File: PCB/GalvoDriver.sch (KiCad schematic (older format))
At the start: 25 parts, among them J1 Screw_Terminal_01x03, J2 Conn_01x03, J3 Conn_01x06_Male, J4 JUMPER_A, J5 JUMPER_B, J6 AudioJack3, J7 Conn_01x03, U1 TL082, U2 MCP4822, U3 TL082

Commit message: Added Laser Module Control + terminal
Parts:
- added J8: Screw_Terminal_01x04, TerminalBlocks_Phoenix:TerminalBlock_Phoenix_MKDS1.5-4pol, symbol Connector:Screw_Terminal_01x04
- added Q1: PN2222A, TO_SOT_Packages_THT:TO-92_Inline_Narrow_Oval, symbol Transistor_BJT:PN2222A
- added R11: 100, Resistors_THT:R_Axial_DIN0207_L6.3mm_D2.5mm_P10.16mm_Horizontal, symbol Device:R_US
- J1: footprint TerminalBlocks_Phoenix:TerminalBlock_Phoenix_PT-3.5mm_3pol -> TerminalBlocks_Phoenix:TerminalBlock_Phoenix_MKDS1.5-3pol
- J3: value Conn_01x06_Male -> Conn_01x07_Male; footprint Pin_Headers:Pin_Header_Straight_1x06_Pitch2.54mm -> Pin_Headers:Pin_Header_Straight_1x07_Pitch2.54mm; symbol Connector:Conn_01x06_Male -> Connector:Conn_01x07_Male
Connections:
- net GND: now also J8.3 (Pin_3), Q1.1 (E)
- new net: J8.1 (Pin_1), Q1.3 (C)
- new net: Q1.2 (B), R11.1
- new net LASER: J3.7 (Pin_7), R11.2
- new net VSS: J8.2 (Pin_2), J8.4 (Pin_4)
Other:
- note added: "Connector Labels:\n1 - 3V3-5V\n2 - CLK\n3 - LATCH\n4 - MOSI\n5 - CS\n6 - LASER\n7 - GND"
- note added: "Connector Labels:\n4 - V+\n3 - GND\n2 - Laser +\n1 - Laser -"
- note added: "Laser Module\nControl"
- note removed: "Connector Labels:\n1 - 3V3-5V\n2 - CLK\n3 - LATCH\n4 - MOSI\n5 - CS\n6 - GND"
- moved on the sheet: J2, J4, J5, J7, R1, R10, R2, R3, R4, R5, R6, R7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

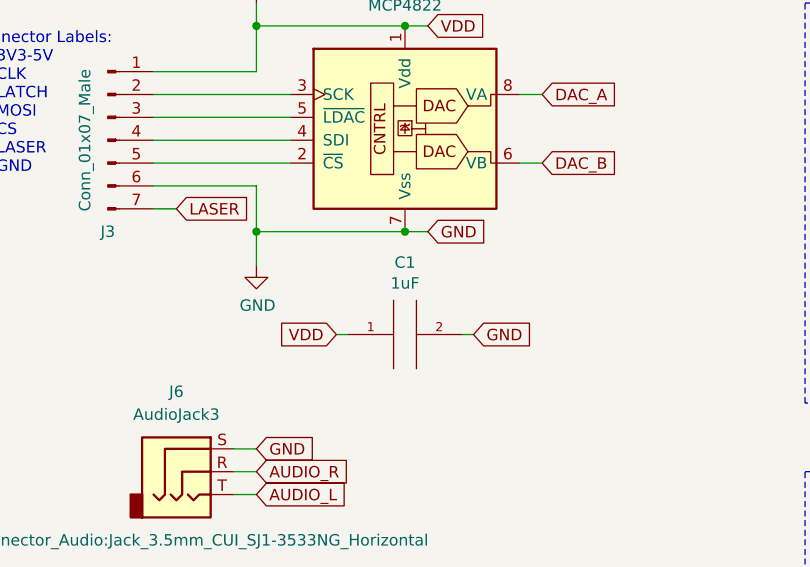
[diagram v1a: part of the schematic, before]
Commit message: Changed decoupling cap value to 0.1uF
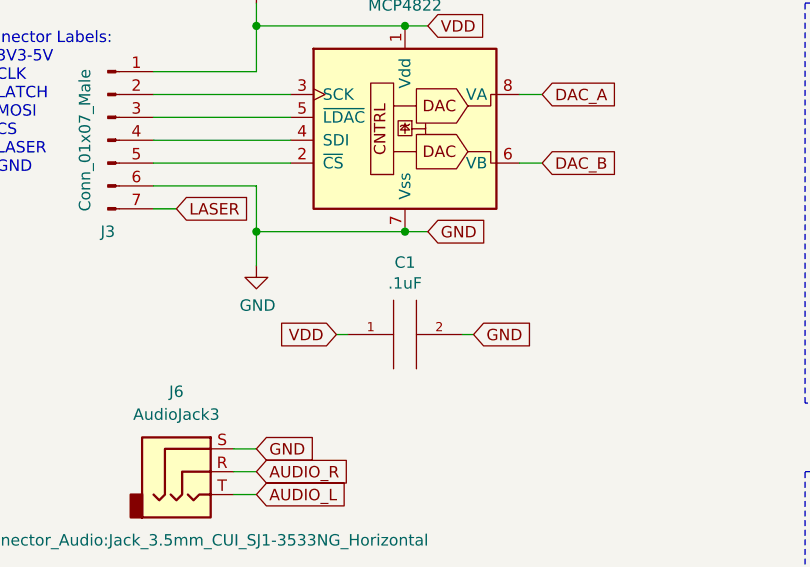
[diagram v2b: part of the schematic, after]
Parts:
- C1: value 1uF -> .1uF; DigiKey (none) -> https://www.digikey.com/product-detail/en/vishay-bc-compone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
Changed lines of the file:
@@
 P 2550 3350
 F 0 "C1" V 2865 3350 50  0000 C CNN
-F 1 "1uF" V 2774 3350 50  0000 C CNN
+F 1 ".1uF" V 2774 3350 50  0000 C CNN
 F 2 "Capacitors_THT:C_Disc_D5.0mm_W2.5mm_P2.50mm" H 2550 3350 50  0001 C CNN
 F 3 "~" H 2550 3350 50  0001 C CNN
+F 4 "https://www.digikey.com/product-detail/en/vishay-bc-components/K104Z15Y5VF5TL2/BC1160CT-ND/286782" V 2550 3350 50  0001 C CNN "DigiKey"
 	1    2550 3350
 	0    -1   -1   0

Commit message: Starting work on PCB changes for v1.1
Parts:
- removed J3: Conn_01x07_Male, Pin_Headers:Pin_Header_Straight_1x07_Pitch2.54mm, symbol Connector:Conn_01x07_Male
- added J?: Conn_01x05_Male, symbol Connector:Conn_01x05_Male
- added U?: 74AHC125, symbol 74ahc125:74AHC125
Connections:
- wire segments 107 -> 110
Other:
- note added: "Connector Labels:\n1 - 3V3-5V\n2 - CLK\n3 - MOSI\n4 - LASER\n5 - GND"
- note removed: "Connector Labels:\n1 - 3V3-5V\n2 - CLK\n3 - LATCH\n4 - MOSI\n5 - CS\n6 - LASER\n7 - GND"
- moved on the sheet: J6
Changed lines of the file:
@@
 Wire Wire Line
 	1700 1450 1600 1450
-$Comp
-L Connector:Conn_01x07_Male J3
-U 1 1 5EFED4AC
-P 1250 2500
-F 0 "J3" H 1250 2100 50  0000 C CNN
-F 1 "Conn_01x07_Male" V 1150 2500 50  0000 C CNN
-F 2 "Pin_Headers:Pin_Header_Straight_1x07_Pitch2.54mm" H 1250 2500 50  0001 C CNN
-F 3 "~" H 1250 2500 50  0001 C CNN
-	1    1250 2500
-	1    0    0    -1
-$EndComp
 Wire Wire Line
 	1900 2200 1900 2000
@@
 	1900 2700 1900 2900
 Wire Wire Line
-	1900 2900 2550 2900
-Text Notes 650  2650 0    50   ~ 0
-Connector Labels:\n1 - 3V3-5V\n2 - CLK\n3 - LATCH\n4 - MOSI\n5 - CS\n6 - LASER\n7 - GND
+	1900 2900 2000 2900
+Text Notes 700  4250 0    50   ~ 0
+Connector Labels:\n1 - 3V3-5V\n2 - CLK\n3 - MOSI\n4 - LASER\n5 - GND
 Text GLabel 8650 2800 0    50   Input ~ 0
 A_ILDA+
@@
 Wire Wire Line
 	2850 3350 2800 3350
-Text GLabel 1900 3950 2    50   Input ~ 0
+Text GLabel 2600 6550 2    50   Input ~ 0
 AUDIO_R
-Text GLabel 1900 3850 2    50   Input ~ 0
-GND
-Text GLabel 1900 4050 2    50   Input ~ 0
+Text GLabel 2600 6450 2    50   Input ~ 0
+GND
+Text GLabel 2600 6650 2    50   Input ~ 0
 AUDIO_L
 Text GLabel 4750 2800 0    50   Input ~ 0
@@
 L Connector:AudioJack3 J6
 U 1 1 5EF780C5
-P 1600 3950
-F 0 "J6" H 1550 4300 50  0000 C CNN
-F 1 "AudioJack3" H 1550 4200 50  0000 C CNN
-F 2 "Connector_Audio:Jack_3.5mm_CUI_SJ1-3533NG_Horizontal" H 1650 3650 50  0000 C CNN
-F 3 "https://www.cuidevices.com/product/resource/sj1-353xng.pdf" H 1600 3950 50  0001 C CNN
-F 4 "https://www.digikey.com/product-detail/en/cui-devices/SJ1-3533NG/CP1-3533NG-ND/738701" H 1600 3950 50  0001 C CNN "DigiKey"
-	1    1600 3950
-	1    0    0    -1
-$EndComp
-Wire Wire Line
-	1900 3850 1800 3850
-Wire Wire Line
-	1800 3950 1900 3950
-Wire Wire Line
-	1900 4050 1800 4050
+P 2300 6550
+F 0 "J6" H 2250 6900 50  0000 C CNN
+F 1 "AudioJack3" H 2250 6800 50  0000 C CNN
+F 2 "Connector_Audio:Jack_3.5mm_CUI_SJ1-3533NG_Horizontal" H 2350 6250 50  0000 C CNN
+F 3 "https://www.cuidevices.com/product/resource/sj1-353xng.pdf" H 2300 6550 50  0001 C CNN
+F 4 "https://www.digikey.com/product-detail/en/cui-devices/SJ1-3533NG/CP1-3533NG-ND/738701" H 2300 6550 50  0001 C CNN "DigiKey"
+	1    2300 6550
+	1    0    0    -1
+$EndComp
+Wire Wire Line
+	2600 6450 2500 6450
+Wire Wire Line
+	2500 6550 2600 6550
+Wire Wire Line
+	2600 6650 2500 6650
 $Comp
 L Connector:Conn_01x03_Male J5
@@
 	1450 2300 2050 2300
 Wire Wire Line
-	1450 2400 2050 2400
-Wire Wire Line
 	1450 2500 2050 2500
-Wire Wire Line
-	1450 2600 2050 2600
 Wire Wire Line
 	1450 2700 1900 2700
@@
 	5750 950  5900 950
 Connection ~ 5900 950
+$Comp
+L 74ahc125:74AHC125 U?
+U 1 1 5F28DEB8
+P 2550 4650
+F 0 "U?" H 2550 5465 50  0000 C CNN
+F 1 "74AHC125" H 2550 5374 50  0000 C CNN
+F 2 "" H 2550 4650 60  0000 C CNN
+F 3 "" H 2550 4650 60  0000 C CNN
+	1    2550 4650
+	1    0    0    -1
+$EndComp
+Wire Wire Line
+	2050 2400 2000 2400
+Wire Wire Line
+	2000 2400 2000 2900
+Connection ~ 2000 2900
+Wire Wire Line
+	2000 2900 2050 2900
+Wire Wire Line
+	2050 2600 2050 2900
+Connection ~ 2050 2900
+Wire Wire Line
+	2050 2900 2550 2900
+$Comp
+L Connector:Conn_01x05_Male J?
+U 1 1 5F2A1C2E
+P 1250 4750
+F 0 "J?" H 1358 5131 50  0000 C CNN
+F 1 "Conn_01x05_Male" H 1358 5040 50  0000 C CNN
+F 2 "" H 1250 4750 50  0001 C CNN
+F 3 "~" H 1250 4750 50  0001 C CNN
+	1    1250 4750
+	1    0    0    -1
+$EndComp
 $EndSCHEMATC

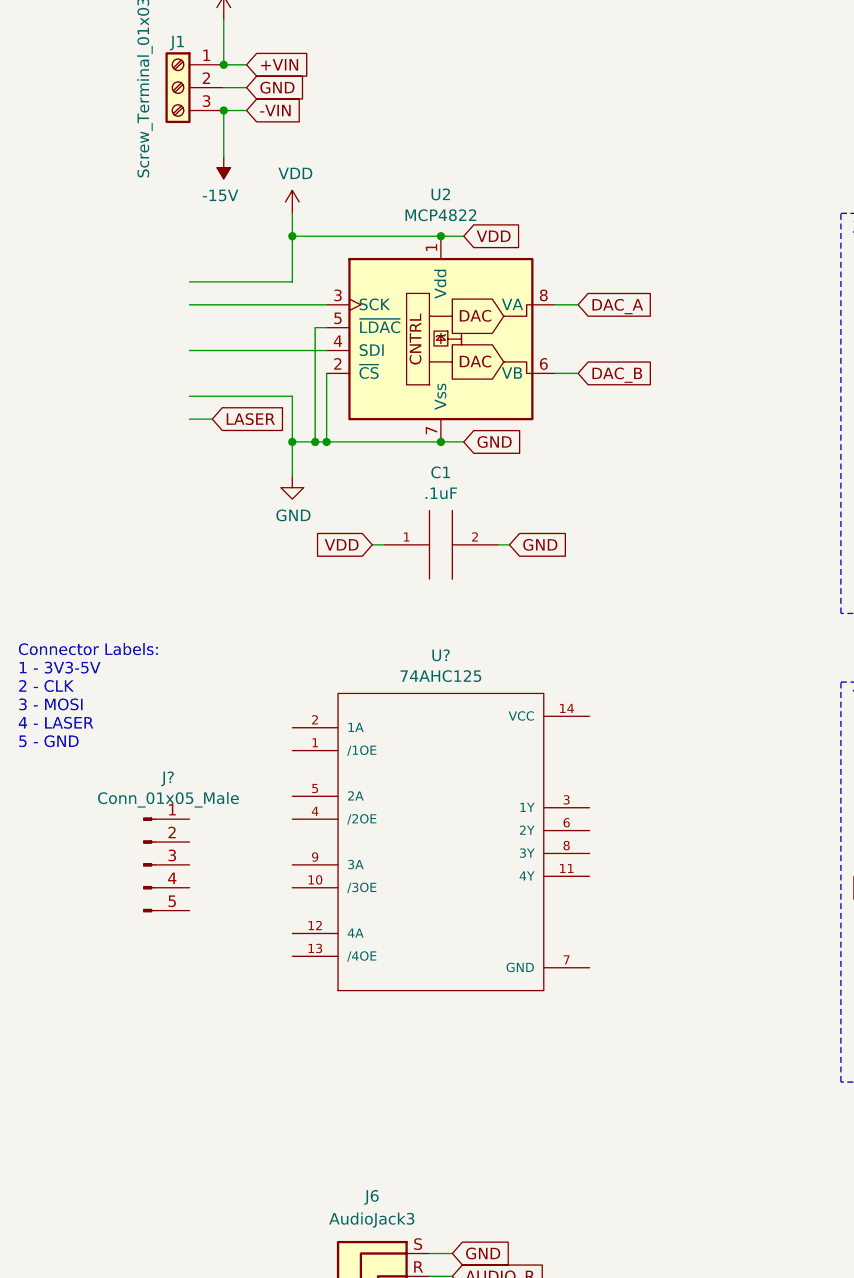
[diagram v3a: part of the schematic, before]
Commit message: Level shifter, thrm. relief, xistor pad, audio jack move
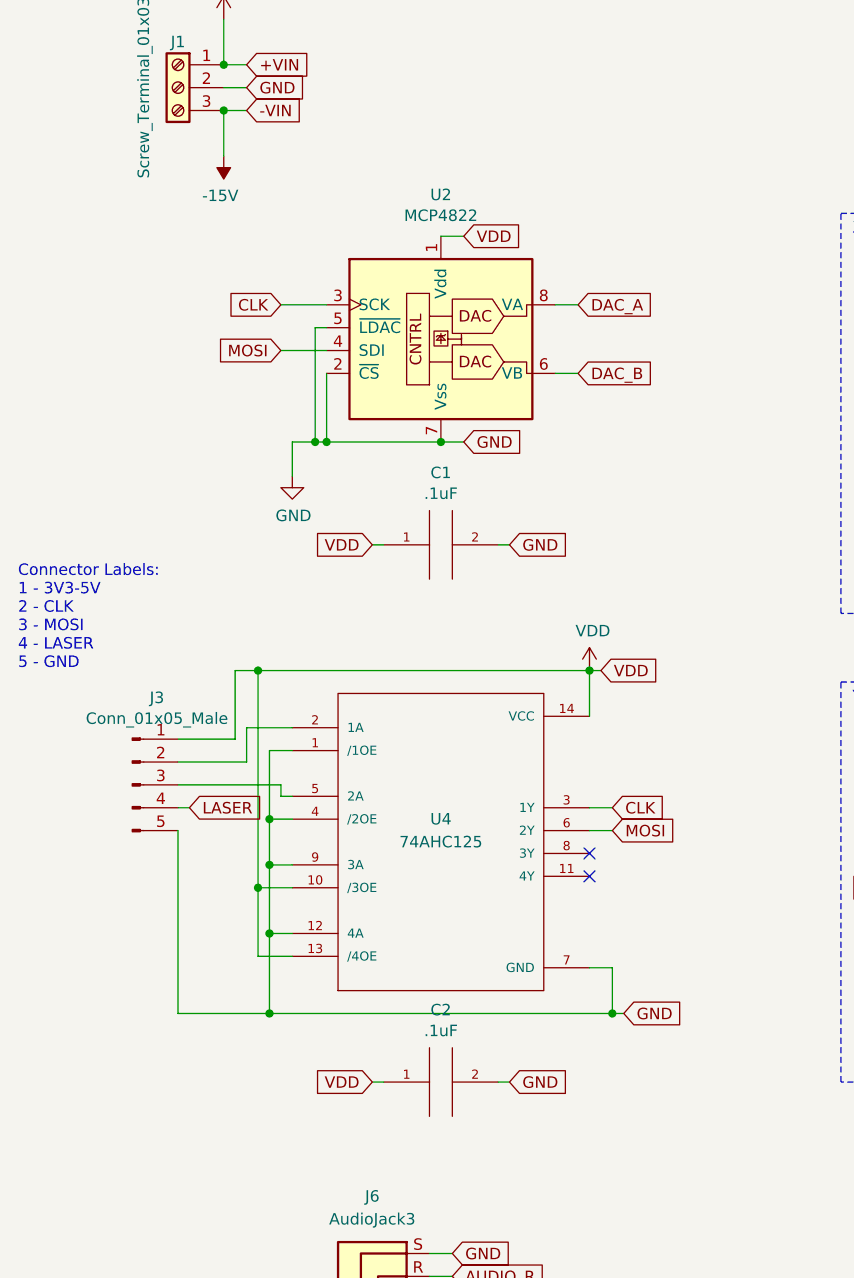
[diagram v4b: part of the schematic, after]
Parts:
- added C2: .1uF, Capacitors_THT:C_Disc_D5.0mm_W2.5mm_P2.50mm, symbol pspice:C
- J3: renamed from J?; footprint (none) -> Pin_Headers:Pin_Header_Straight_1x05_Pitch2.54mm
- Q1: footprint TO_SOT_Packages_THT:TO-92_Inline_Narrow_Oval -> TO_SOT_Packages_THT:TO-92_Inline_Wide
- U4: renamed from U?; footprint (none) -> Housings_DIP:DIP-14_W7.62mm_Socket; DigiKey (none) -> https://www.digikey.com/product-detail/en/texas-instruments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
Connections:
- net labels added: CLK, MOSI
- wire segments 110 -> 138
- no-connect marks 2 -> 4
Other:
- moved on the sheet: J3
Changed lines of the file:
@@
 	1700 1450 1600 1450
 Wire Wire Line
-	1900 2200 1900 2000
-Wire Wire Line
-	1900 2000 2550 2000
-Wire Wire Line
-	1900 2700 1900 2900
-Wire Wire Line
 	1900 2900 2000 2900
-Text Notes 700  4250 0    50   ~ 0
+Text Notes 700  3900 0    50   ~ 0
 Connector Labels:\n1 - 3V3-5V\n2 - CLK\n3 - MOSI\n4 - LASER\n5 - GND
 Text GLabel 8650 2800 0    50   Input ~ 0
@@
 L power:VDD #PWR0101
 U 1 1 5F007EE1
-P 1900 1900
-F 0 "#PWR0101" H 1900 1750 50  0001 C CNN
-F 1 "VDD" H 1915 2073 50  0000 C CNN
-F 2 "" H 1900 1900 50  0001 C CNN
-F 3 "" H 1900 1900 50  0001 C CNN
-	1    1900 1900
+P 3200 3900
+F 0 "#PWR0101" H 3200 3750 50  0001 C CNN
+F 1 "VDD" H 3215 4073 50  0000 C CNN
+F 2 "" H 3200 3900 50  0001 C CNN
+F 3 "" H 3200 3900 50  0001 C CNN
+	1    3200 3900
 	1    0    0    -1
 $EndComp
@@
 Wire Wire Line
 	1900 3050 1900 2900
-Connection ~ 1900 2900
-Wire Wire Line
-	1900 1900 1900 2000
-Connection ~ 1900 2000
 Wire Wire Line
 	5800 3200 6400 3200
@@
 Wire Wire Line
 	2650 2000 2550 2000
-Connection ~ 2550 2000
 Text GLabel 2250 3350 0    50   Input ~ 0
 VDD
@@
 Wire Wire Line
 	8650 5050 8750 5050
-Text GLabel 1550 2800 2    50   Input ~ 0
-LASER
-Wire Wire Line
-	1450 2200 1900 2200
-Wire Wire Line
-	1450 2300 2050 2300
-Wire Wire Line
-	1450 2500 2050 2500
-Wire Wire Line
-	1450 2700 1900 2700
-Wire Wire Line
-	1550 2800 1450 2800
 $Comp
 L Connector:Screw_Terminal_01x04 J8
@@
 F 0 "Q1" H 6290 1446 50  0000 L CNN
 F 1 "PN2222A" H 6290 1355 50  0000 L CNN
-F 2 "TO_SOT_Packages_THT:TO-92_Inline_Narrow_Oval" H 6300 1325 50  0001 L CIN
+F 2 "TO_SOT_Packages_THT:TO-92_Inline_Wide" H 6300 1325 50  0001 L CIN
 F 3 "http://www.fairchildsemi.com/ds/PN/PN2222A.pdf" H 6100 1400 50  0001 L CNN
 	1    6100 1400
@@
 Connection ~ 5900 950
 $Comp
-L 74ahc125:74AHC125 U?
+L 74ahc125:74AHC125 U4
 U 1 1 5F28DEB8
 P 2550 4650
-F 0 "U?" H 2550 5465 50  0000 C CNN
-F 1 "74AHC125" H 2550 5374 50  0000 C CNN
-F 2 "" H 2550 4650 60  0000 C CNN
-F 3 "" H 2550 4650 60  0000 C CNN
+F 0 "U4" H 2550 4750 50  0000 C CNN
+F 1 "74AHC125" H 2550 4650 50  0000 C CNN
+F 2 "Housings_DIP:DIP-14_W7.62mm_Socket" H 2550 4650 60  0001 C CNN
+F 3 "http://www.ti.com/general/docs/suppproductinfo.tsp?distId=10&gotoUrl=http%3A%2F%2Fwww.ti.com%2Flit%2Fgpn%2Fsn74ahc125" H 2550 4650 60  0001 C CNN
+F 4 "https://www.digikey.com/product-detail/en/texas-instruments/SN74AHC125N/296-4531-5-ND/375724" H 2550 4650 50  0001 C CNN "DigiKey"
 	1    2550 4650
 	1    0    0    -1
@@
 	2050 2900 2550 2900
 $Comp
-L Connector:Conn_01x05_Male J?
+L Connector:Conn_01x05_Male J3
 U 1 1 5F2A1C2E
-P 1250 4750
-F 0 "J?" H 1358 5131 50  0000 C CNN
-F 1 "Conn_01x05_Male" H 1358 5040 50  0000 C CNN
-F 2 "" H 1250 4750 50  0001 C CNN
-F 3 "~" H 1250 4750 50  0001 C CNN
-	1    1250 4750
-	1    0    0    -1
-$EndComp
+P 1200 4400
+F 0 "J3" H 1308 4781 50  0000 C CNN
+F 1 "Conn_01x05_Male" H 1308 4690 50  0000 C CNN
+F 2 "Pin_Headers:Pin_Header_Straight_1x05_Pitch2.54mm" H 1200 4400 50  0001 C CNN
+F 3 "~" H 1200 4400 50  0001 C CNN
+	1    1200 4400
+	1    0    0    -1
+$EndComp
+Wire Wire Line
+	1900 4250 1800 4250
+Wire Wire Line
+	1800 5400 3300 5400
+Wire Wire Line
+	3300 5400 3300 5200
+Wire Wire Line
+	3300 5200 3200 5200
+Text GLabel 3350 5400 2    50   Input ~ 0
+GND
+Wire Wire Line
+	3300 5400 3350 5400
+Connection ~ 3300 5400
+Wire Wire Line
+	1800 4250 1800 4550
+Wire Wire Line
+	3200 4100 3200 3900
+Wire Wire Line
+	1750 5150 1900 5150
+Wire Wire Line
+	1900 4850 1750 4850
+Wire Wire Line
+	1750 4850 1750 5150
+Wire Wire Line
+	1800 4550 1900 4550
+Connection ~ 1800 4550
+Wire Wire Line
+	1800 4550 1800 4750
+Wire Wire Line
+	1400 4300 1700 4300
+Wire Wire Line
+	1700 4300 1700 4150
+Wire Wire Line
+	1700 4150 1900 4150
+Text GLabel 1450 4500 2    50   Input ~ 0
+LASER
+Wire Wire Line
+	1400 4600 1400 5400
+Wire Wire Line
+	1400 5400 1800 5400
+Connection ~ 1800 5400
+Wire Wire Line
+	1400 4200 1650 4200
+Wire Wire Line
+	1650 4200 1650 3900
+Text GLabel 3250 3900 2    50   Input ~ 0
+VDD
+Wire Wire Line
+	3200 3900 3250 3900
+Connection ~ 3200 3900
+NoConn ~ 3200 4800
+NoConn ~ 3200 4700
+Connection ~ 1750 4850
+Wire Wire Line
+	1650 3900 1750 3900
+Wire Wire Line
+	3200 3900 1750 3900
+Connection ~ 1750 3900
+Wire Wire Line
+	1750 3900 1750 4850
+Wire Wire Line
+	1400 4500 1450 4500
+Wire Wire Line
+	1850 4400 1850 4450
+Wire Wire Line
+	1850 4450 1900 4450
+Wire Wire Line
+	1400 4400 1850 4400
+Text GLabel 3300 4500 2    50   Input ~ 0
+CLK
+Wire Wire Line
+	3200 4500 3300 4500
+Text GLabel 3300 4600 2    50   Input ~ 0
+MOSI
+Wire Wire Line
+	3300 4600 3200 4600
+Text GLabel 1850 2300 0    50   Input ~ 0
+CLK
+Text GLabel 1850 2500 0    50   Input ~ 0
+MOSI
+Wire Wire Line
+	1850 2300 2050 2300
+Wire Wire Line
+	1850 2500 2050 2500
+Wire Wire Line
+	1900 4750 1800 4750
+Connection ~ 1800 4750
+Wire Wire Line
+	1800 4750 1800 5050
+Wire Wire Line
+	1900 5050 1800 5050
+Connection ~ 1800 5050
+Wire Wire Line
+	1800 5050 1800 5400
+$Comp
+L pspice:C C2
+U 1 1 5F4AEBB5
+P 2550 5700
+F 0 "C2" V 2865 5700 50  0000 C CNN
+F 1 ".1uF" V 2774 5700 50  0000 C CNN
+F 2 "Capacitors_THT:C_Disc_D5.0mm_W2.5mm_P2.50mm" H 2550 5700 50  0001 C CNN
+F 3 "~" H 2550 5700 50  0001 C CNN
+F 4 "https://www.digikey.com/product-detail/en/vishay-bc-components/K104Z15Y5VF5TL2/BC1160CT-ND/286782" V 2550 5700 50  0001 C CNN "DigiKey"
+	1    2550 5700
+	0    -1   -1   0
+$EndComp
+Text GLabel 2250 5700 0    50   Input ~ 0
+VDD
+Text GLabel 2850 5700 2    50   Input ~ 0
+GND
+Wire Wire Line
+	2250 5700 2300 5700
+Wire Wire Line
+	2850 5700 2800 5700
 $EndSCHEMATC
